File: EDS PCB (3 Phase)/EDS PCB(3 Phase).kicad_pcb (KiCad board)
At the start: 2 copper layers, 219.5 x 153.5 mm, 23 parts, among them P1 EDS Pad, P3 EDS Pad

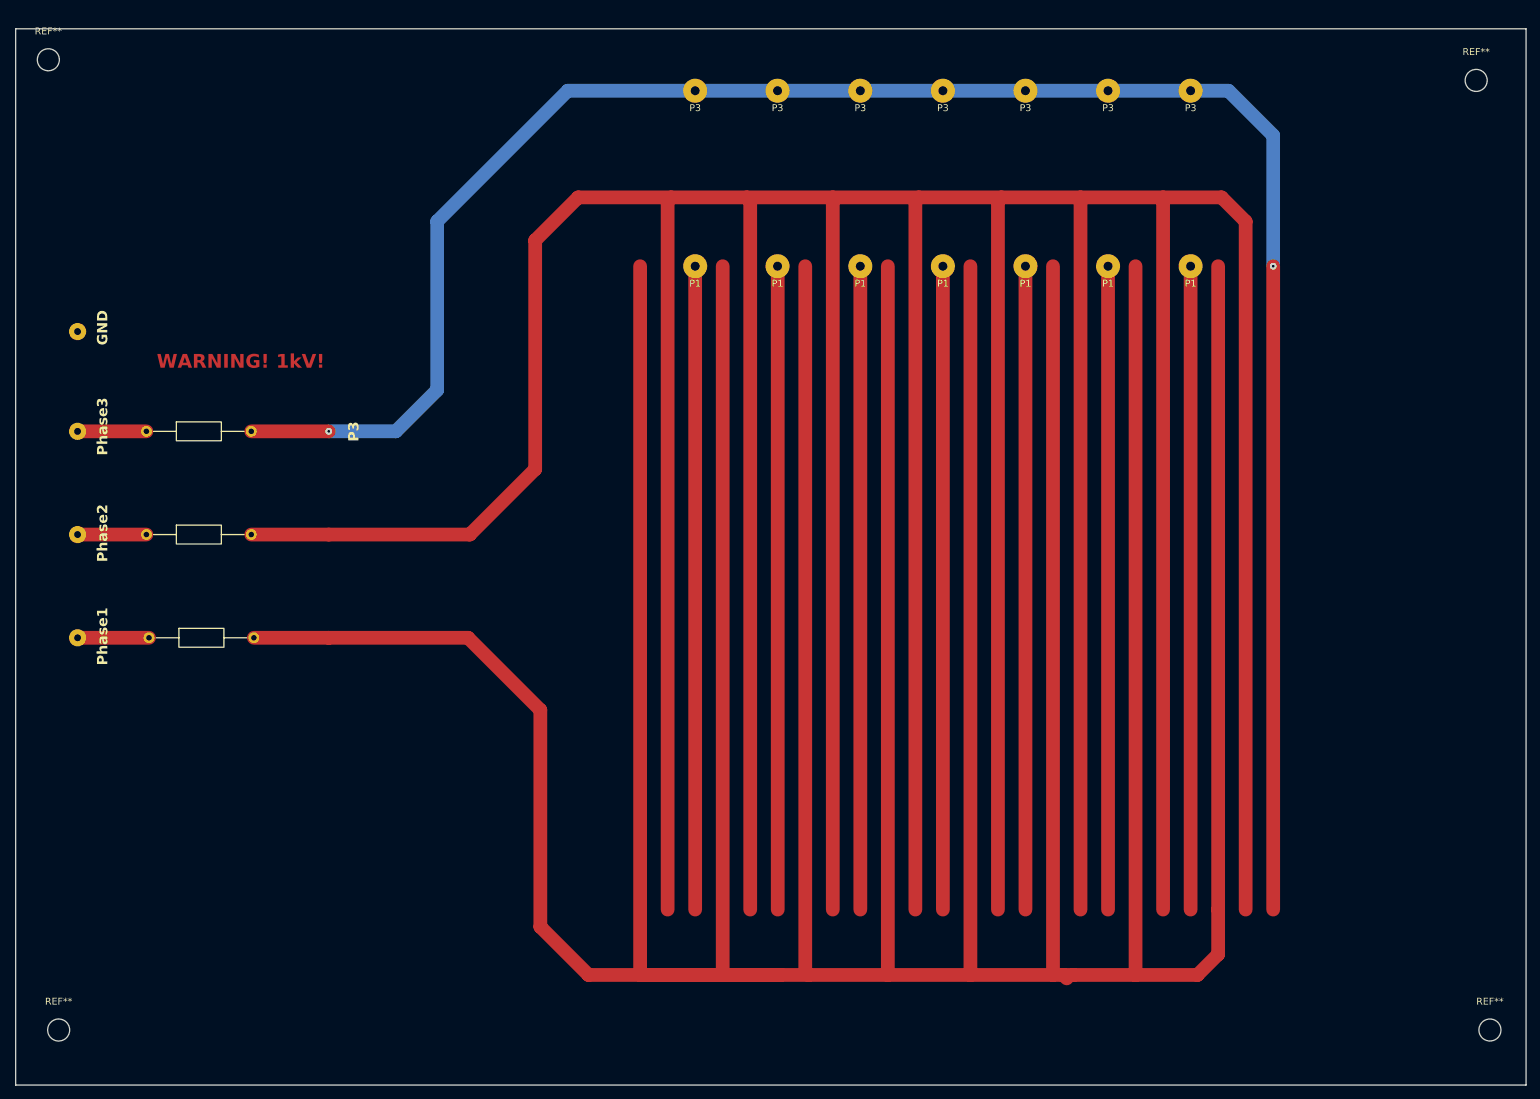
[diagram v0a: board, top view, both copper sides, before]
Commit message: Two-Phase and Three-Phase EDS PCBs.
I changed the Two-Phase and Three-Phase EDS PCBs. They just need minor changes now
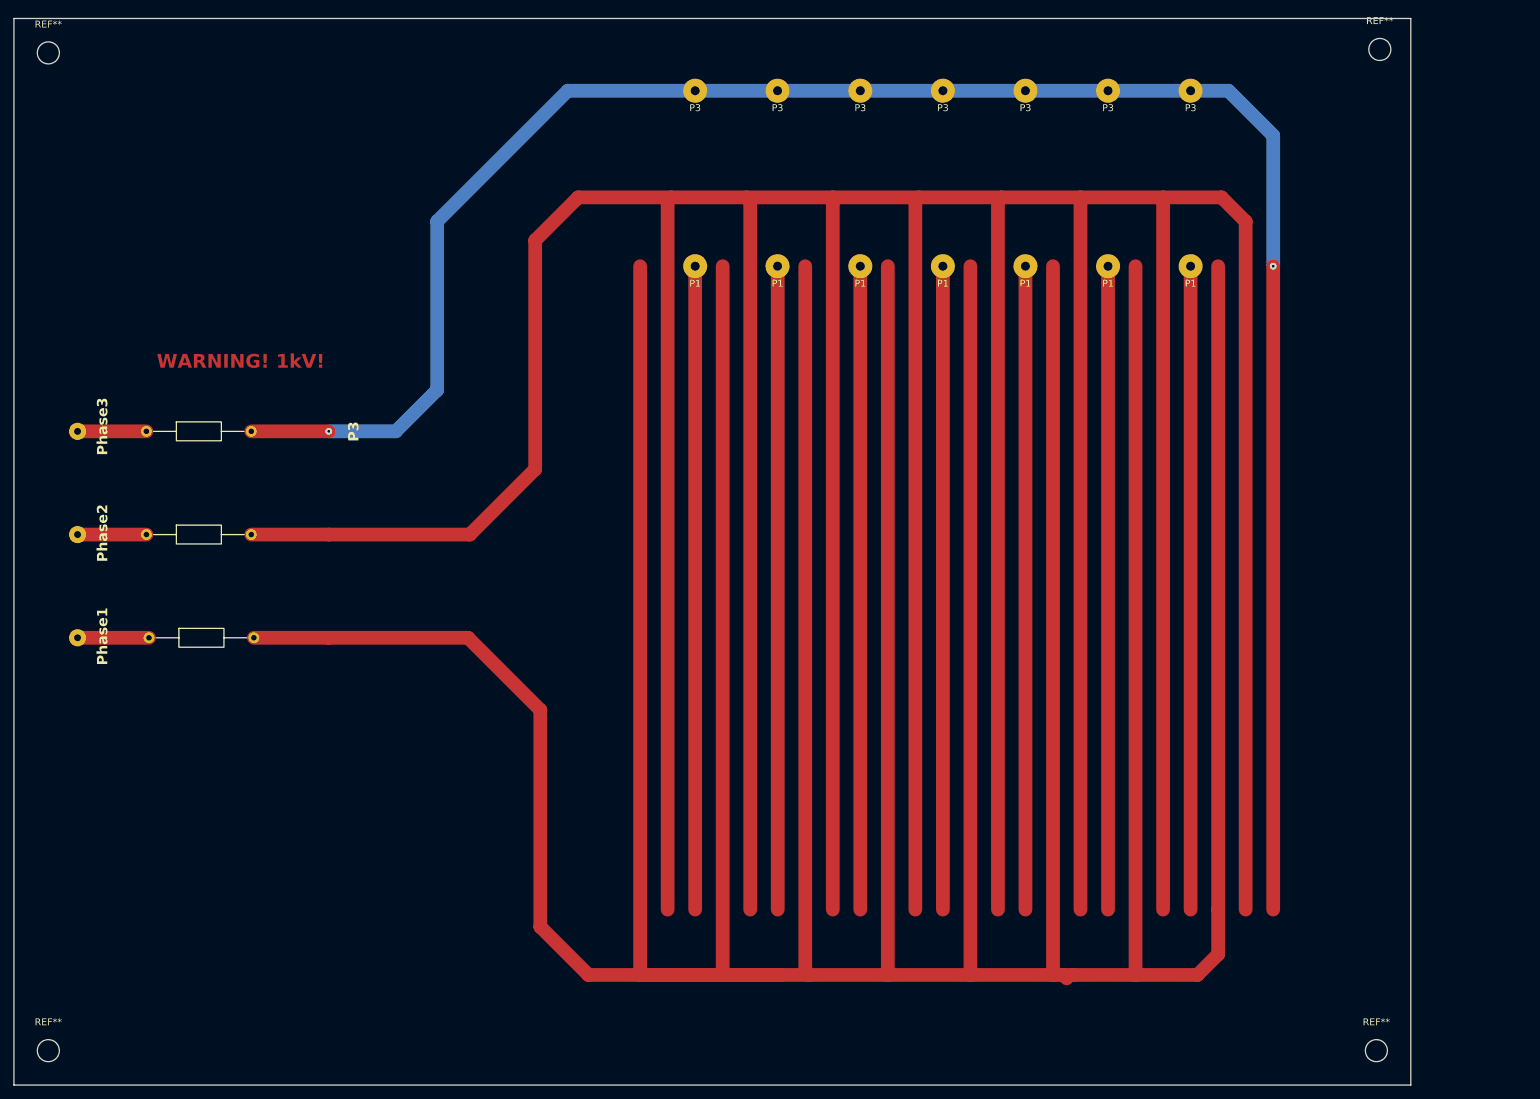
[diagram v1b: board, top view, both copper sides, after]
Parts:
- removed ?: , clipboard:bf32c9e1-eea9-421a-b75f-750c3fb07239
- moved REF** 16.8 mm to (223.0, 170.0)
- moved REF** 14.7 mm to (223.5, 24.5)
- moved REF** 3.35 mm to (30.0, 170.0)
- moved REF** 1.00 mm to (30.0, 25.0)
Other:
- board size 219.5 x 153.5 mm -> 203 x 155 mm
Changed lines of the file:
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@@
-		(embedded_fonts no)
-	)
-	(footprint "clipboard:bf32c9e1-eea9-421a-b75f-750c3fb07239"
-		(layer "F.Cu")
-		(at 34.25 65.5 90)
-		(property "Reference" ""
-			(at 0 0 90)
-			(layer "F.SilkS")
-			(effects
-				(font
-					(size 1.27 1.27)
-					(thickness 0.15)
-				)
-			)
-		)
-		(property "Value" ""
-			(at 0 0 90)
-			(layer "F.Fab")
-			(effects
-				(font
-					(size 1.27 1.27)
-					(thickness 0.15)
-				)
-			)
-		)
-		(property "Datasheet" ""
-			(at 0 0 90)
-			(layer "F.Fab")
-			(hide yes)
-			(effects
-				(font
-					(size 1.27 1.27)
-					(thickness 0.15)
-				)
-			)
-		)
-		(property "Description" ""
-			(at 0 0 90)
-			(layer "F.Fab")
-			(hide yes)
-			(effects
-				(font
-					(size 1.27 1.27)
-					(thickness 0.15)
-				)
-			)
-		)
-		(fp_text user "GND"
-			(at -2 4.5 90)
-			(unlocked yes)
-			(layer "F.SilkS")
-			(effects
-				(font
-					(size 1.5 1.5)
-					(thickness 0.25)
-					(bold yes)
-				)
-				(justify left bottom)
-			)
-		)
-		(pad "1" thru_hole circle
-			(at 0 0 90)
-			(size 2.5 2.5)
-			(drill 1)
-			(layers "*.Cu" "*.Mask")
-			(remove_unused_layers no)
-		)
 		(embedded_fonts no)
 	)
 	(footprint "MountingHole:MountingHole_3.2mm_M3"
 		(layer "F.Cu")
-		(at 239.5 167)
+		(at 223 170)
 		(descr "Mounting Hole 3.2mm, M3, no annular, generated by kicad-footprint-generator mountinghole.py")
 		(tags "mountinghole M3")
@@
 	(footprint "MountingHole:MountingHole_3.2mm_M3"
 		(layer "F.Cu")
-		(at 237.5 29)
+		(at 223.5 24.5)
 		(descr "Mounting Hole 3.2mm, M3, no annular, generated by kicad-footprint-generator mountinghole.py")
 		(tags "mountinghole M3")
@@
 	(footprint "MountingHole:MountingHole_3.2mm_M3"
 		(layer "F.Cu")
-		(at 31.5 167)
+		(at 30 170)
 		(descr "Mounting Hole 3.2mm, M3, no annular, generated by kicad-footprint-generator mountinghole.py")
 		(tags "mountinghole M3")
@@
 	(footprint "MountingHole:MountingHole_3.2mm_M3"
 		(layer "F.Cu")
-		(at 30 26)
+		(at 30 25)
 		(descr "Mounting Hole 3.2mm, M3, no annular, generated by kicad-footprint-generator mountinghole.py")
 		(tags "mountinghole M3")
@@
 	)
 	(gr_rect
-		(start 25.25 21.5)
-		(end 244.75 175)
+		(start 25 20)
+		(end 228 175)
 		(stroke
 			(width 0.05)

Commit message: Confirmed Spacing
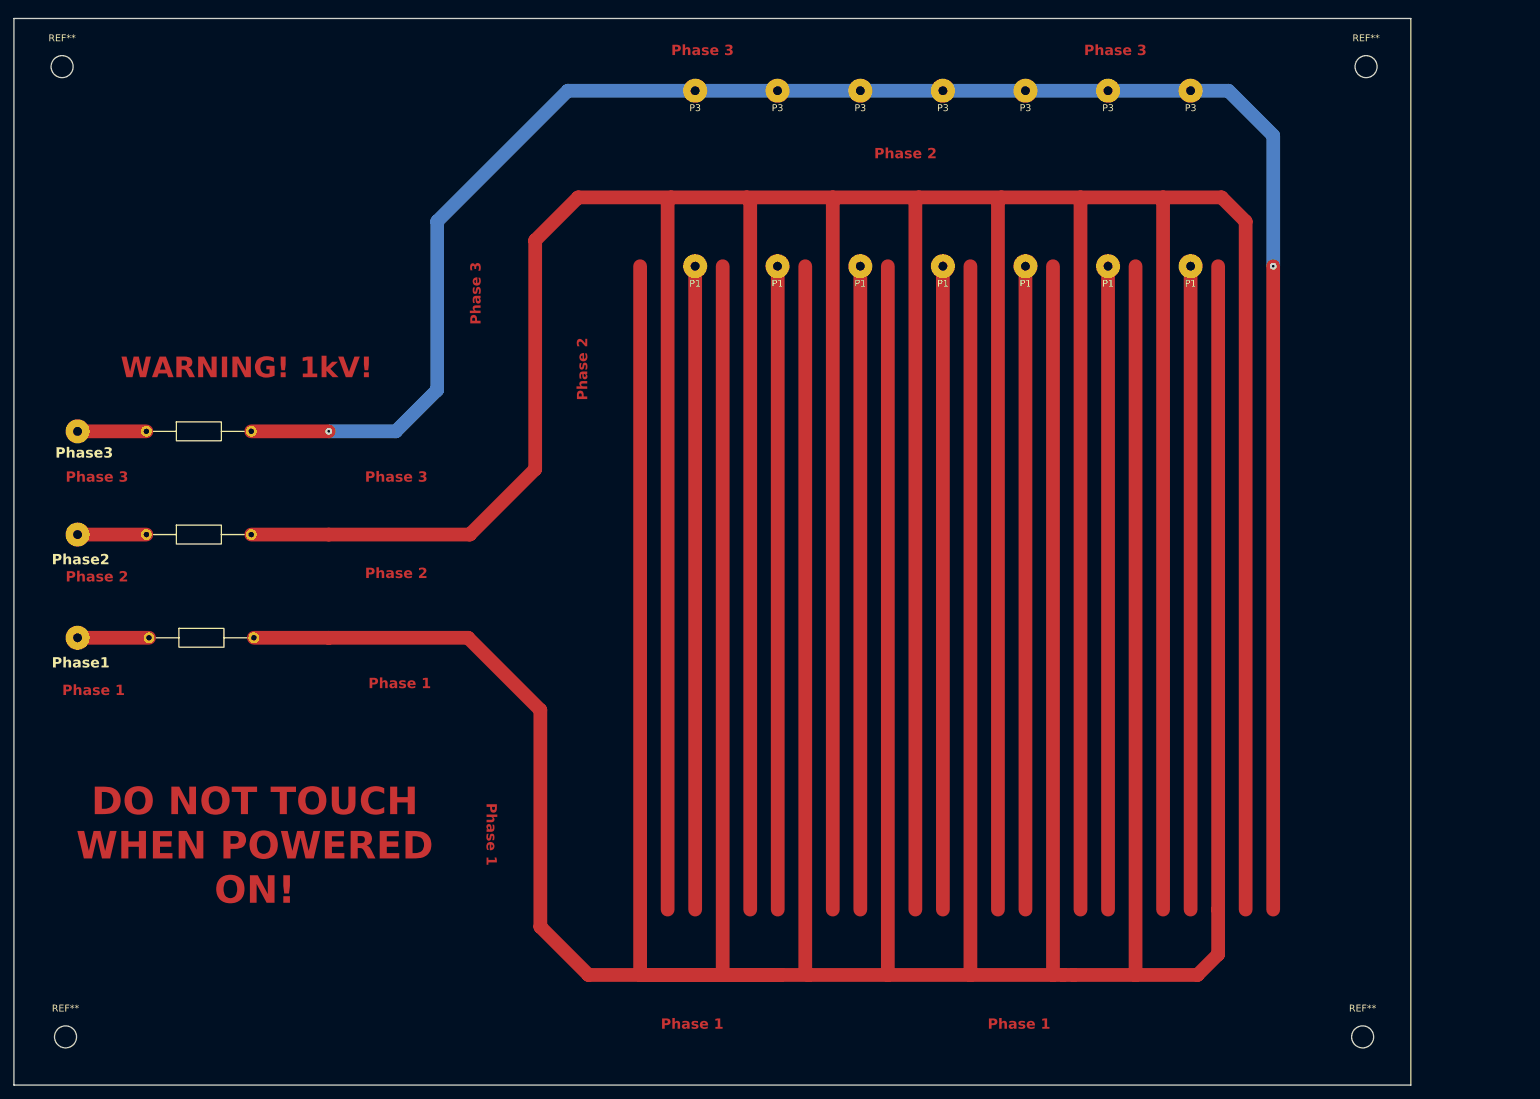
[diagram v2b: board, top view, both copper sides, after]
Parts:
- moved REF** 3.20 mm to (221.5, 27.0)
- moved REF** 3.20 mm to (32.5, 168.0)
- moved REF** 2.83 mm to (221.0, 168.0)
- moved REF** 2.83 mm to (32.0, 27.0)
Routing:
- net Phase1: track 1022.5 -> 1021.8 mm
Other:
- board text added: "DO NOT TOUCH WHEN POWERED ON!"
- board text added: "Phase 1"
- board text added: "Phase 2"
- board text added: "Phase 3"
- board text removed: "P3"
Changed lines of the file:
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@@
 	(footprint "MountingHole:MountingHole_3.2mm_M3"
 		(layer "F.Cu")
-		(at 223 170)
+		(at 221 168)
 		(descr "Mounting Hole 3.2mm, M3, no annular, generated by kicad-footprint-generator mountinghole.py")
 		(tags "mountinghole M3")
@@
 			(layer "F.CrtYd")
 		)
-		(fp_text user "${REFERENCE}"
-			(at 0 0 0)
-			(layer "F.Fab")
-			(effects
-				(font
-					(size 1 1)
-					(thickness 0.15)
-				)
-			)
-		)
 		(pad "" np_thru_hole circle
 			(at 0 0)
@@
 	(footprint "MountingHole:MountingHole_3.2mm_M3"
 		(layer "F.Cu")
-		(at 223.5 24.5)
+		(at 221.5 27)
 		(descr "Mounting Hole 3.2mm, M3, no annular, generated by kicad-footprint-generator mountinghole.py")
 		(tags "mountinghole M3")
@@
 	(footprint "MountingHole:MountingHole_3.2mm_M3"
 		(layer "F.Cu")
-		(at 30 170)
+		(at 32.5 168)
 		(descr "Mounting Hole 3.2mm, M3, no annular, generated by kicad-footprint-generator mountinghole.py")
 		(tags "mountinghole M3")
@@
 		(attr smd)
 		(fp_text user "Phase3"
-			(at 26.5 4.5 90)
+			(at 26 -3.25 0)
 			(unlocked yes)
 			(layer "F.SilkS")
@@
 		)
 		(fp_text user "Phase1"
-			(at -4 4.5 90)
+			(at -4.5 -3.75 0)
 			(unlocked yes)
 			(layer "F.SilkS")
@@
 		)
 		(fp_text user "Phase2"
-			(at 11 4.5 90)
+			(at 10.5 -3.75 0)
 			(unlocked yes)
 			(layer "F.SilkS")
@@
 		(pad "1" thru_hole circle
 			(at 0 0 90)
-			(size 2.5 2.5)
-			(drill 1)
+			(size 3.5 3.5)
+			(drill 1.3)
 			(layers "*.Cu" "*.Mask")
 			(remove_unused_layers no)
@@
 		(pad "1" thru_hole circle
 			(at 15 0 90)
-			(size 2.5 2.5)
-			(drill 1)
+			(size 3.5 3.5)
+			(drill 1.3)
 			(layers "*.Cu" "*.Mask")
 			(remove_unused_layers no)
@@
 		(pad "1" thru_hole circle
 			(at 30 0 90)
-			(size 2.5 2.5)
-			(drill 1)
+			(size 3.5 3.5)
+			(drill 1.3)
 			(layers "*.Cu" "*.Mask")
 			(remove_unused_layers no)
@@
 	(footprint "MountingHole:MountingHole_3.2mm_M3"
 		(layer "F.Cu")
-		(at 30 25)
+		(at 32 27)
 		(descr "Mounting Hole 3.2mm, M3, no annular, generated by kicad-footprint-generator mountinghole.py")
 		(tags "mountinghole M3")
@@
 	)
 	(image
-		(at 55.75 57.5)
+		(at 56.071979 47.5)
 		(layer "F.Cu")
-		(scale 0.211671)
+		(scale 0.490709)
 		(data "iVBORw0KGgoAAAANSUhEUgAABLAAAASwCAYAAADrIbPPAAAABGdBTUEAALGPC/xhBQAAACBjSFJN"
 			"AAB6JgAAgIQAAPoAAACA6AAAdTAAAOpgAAA6mAAAF3CculE8AAAABmJLR0QA/wD/AP+gvaeTAACA"
@@
 		)
 	)
+	(gr_text "Phase 1\n"
+		(at 119 167 0)
+		(layer "F.Cu")
+		(effects
+			(font
+				(size 1.5 1.5)
+				(thickness 0.3)
+				(bold yes)
+			)
+			(justify left bottom)
+		)
+	)
+	(gr_text "Phase 2"
+		(at 108.5 75.5 90)
+		(layer "F.Cu")
+		(effects
+			(font
+				(size 1.5 1.5)
+				(thickness 0.3)
+				(bold yes)
+			)
+			(justify left bottom)
+		)
+	)
+	(gr_text "Phase 1\n"
+		(at 166.5 167 0)
+		(layer "F.Cu")
+		(effects
+			(font
+				(size 1.5 1.5)
+				(thickness 0.3)
+				(bold yes)
+			)
+			(justify left bottom)
+		)
+	)
+	(gr_text "Phase 1\n"
+		(at 76.5 117.5 0)
+		(layer "F.Cu")
+		(effects
+			(font
+				(size 1.5 1.5)
+				(thickness 0.3)
+				(bold yes)
+			)
+			(justify left bottom)
+		)
+	)
+	(gr_text "Phase 2"
+		(at 150 40.5 0)
+		(layer "F.Cu")
+		(effects
+			(font
+				(size 1.5 1.5)
+				(thickness 0.3)
+				(bold yes)
+			)
+			(justify left bottom)
+		)
+	)
+	(gr_text "Phase 3"
+		(at 120.5 25.5 0)
+		(layer "F.Cu")
+		(effects
+			(font
+				(size 1.5 1.5)
+				(thickness 0.3)
+				(bold yes)
+			)
+			(justify left bottom)
+		)
+	)
+	(gr_text "Phase 1\n"
+		(at 32 118.5 0)
+		(layer "F.Cu")
+		(effects
+			(font
+				(size 1.5 1.5)
+				(thickness 0.3)
+				(bold yes)
+			)
+			(justify left bottom)
+		)
+	)
+	(gr_text "Phase 2"
+		(at 32.5 102 0)
+		(layer "F.Cu")
+		(effects
+			(font
+				(size 1.5 1.5)
+				(thickness 0.3)
+				(bold yes)
+			)
+			(justify left bottom)
+		)
+	)
+	(gr_text "Phase 2"
+		(at 76 101.5 0)
+		(layer "F.Cu")
+		(effects
+			(font
+				(size 1.5 1.5)
+				(thickness 0.3)
+				(bold yes)
+			)
+			(justify left bottom)
+		)
+	)
 	(gr_text "WARNING! 1kV!"
-		(at 45.75 71 0)
+		(at 40.5 72.5 0)
 		(layer "F.Cu")
 		(effects
 			(font
-				(size 2 2)
+				(size 3 3)
 				(thickness 0.35)
 				(bold yes)
@@
 		)
 	)
-	(gr_text "P3"
-		(at 75.25 81.5 90)
-		(layer "F.SilkS")
+	(gr_text "Phase 3"
+		(at 32.5 87.5 0)
+		(layer "F.Cu")
+		(effects
+			(font
+				(size 1.5 1.5)
+				(thickness 0.3)
+				(bold yes)
+			)
+			(justify left bottom)
+		)
+	)
+	(gr_text "Phase 3"
+		(at 76 87.5 0)
+		(layer "F.Cu")
 		(effects
 			(font
 				(size 1.5 1.5)
-				(thickness 0.25)
+				(thickness 0.3)
 				(bold yes)
 			)
@@
 		)
 	)
+	(gr_text "Phase 3"
+		(at 180.5 25.5 0)
+		(layer "F.Cu")
+		(effects
+			(font
+				(size 1.5 1.5)
+				(thickness 0.3)
+				(bold yes)
+			)
+			(justify left bottom)
+		)
+	)
+	(gr_text "Phase 1\n"
+		(at 93.5 134 270)
+		(layer "F.Cu")
+		(effects
+			(font
+				(size 1.5 1.5)
+				(thickness 0.3)
+				(bold yes)
+			)
+			(justify left bottom)
+		)
+	)
+	(gr_text "Phase 3"
+		(at 93 64.5 90)
+		(layer "F.Cu")
+		(effects
+			(font
+				(size 1.5 1.5)
+				(thickness 0.3)
+				(bold yes)
+			)
+			(justify left bottom)
+		)
+	)
+	(gr_text "DO NOT TOUCH \nWHEN POWERED \nON!"
+		(at 60 149 0)
+		(layer "F.Cu")
+		(effects
+			(font
+				(size 4 4)
+				(thickness 1)
+				(bold yes)
+			)
+			(justify bottom)
+		)
+	)
 	(segment
 		(start 34.25 80)
@@
 		(width 2)
 		(layer "F.Cu")
-		(net 1)
-	)
-	(segment
-		(start 178 159.5)
-		(end 177.5 159)
-		(width 2)
-		(layer "F.Cu")
